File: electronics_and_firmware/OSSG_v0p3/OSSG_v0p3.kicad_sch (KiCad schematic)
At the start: 69 parts, among them IC1 DW01A, J1 USB_B_Micro, J2 External PDM Mic Input, Q1 FS8205A, Q2 Q_NPN_BEC, Q3 Q_NPN_BEC, SW1 SW_SPST, U1 ESP32-PICO-D4, U2 TP4056, U3 XC6222B331MRG, U4 CH9102F, U5 CL7809SS, U6 MP23DB01HPTR

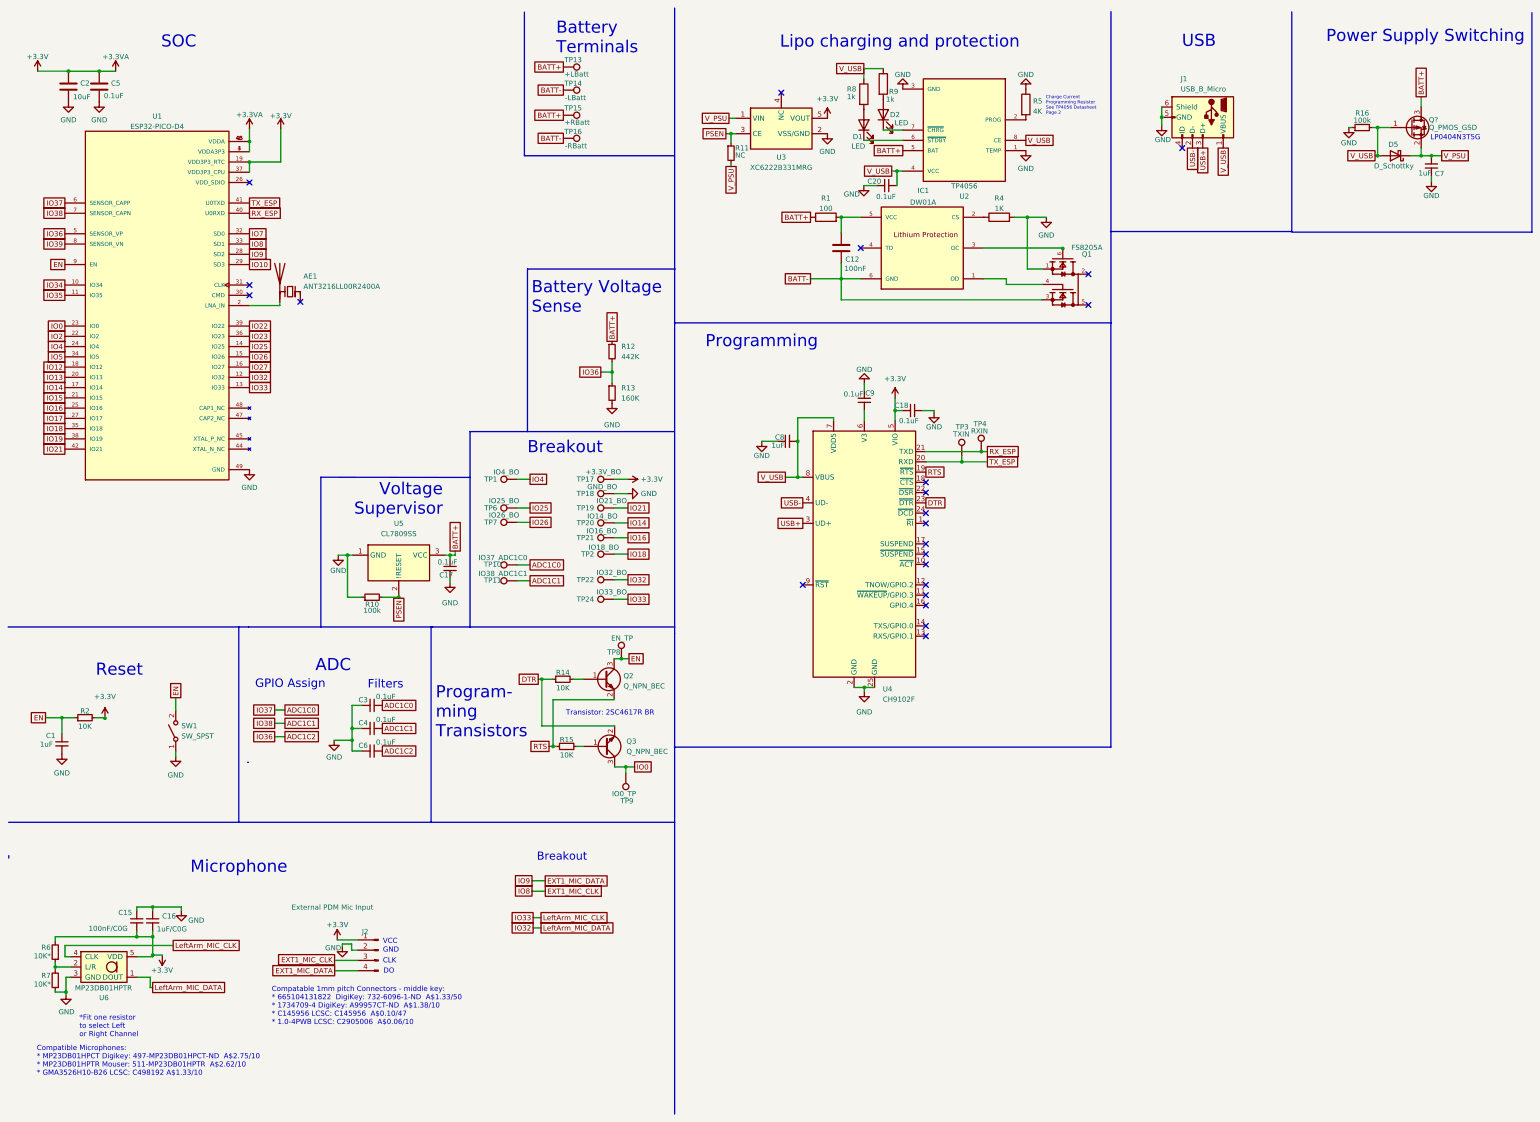
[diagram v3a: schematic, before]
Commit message: change to new LDO, change voltage supervisor, inspect board, slight silk screen changes
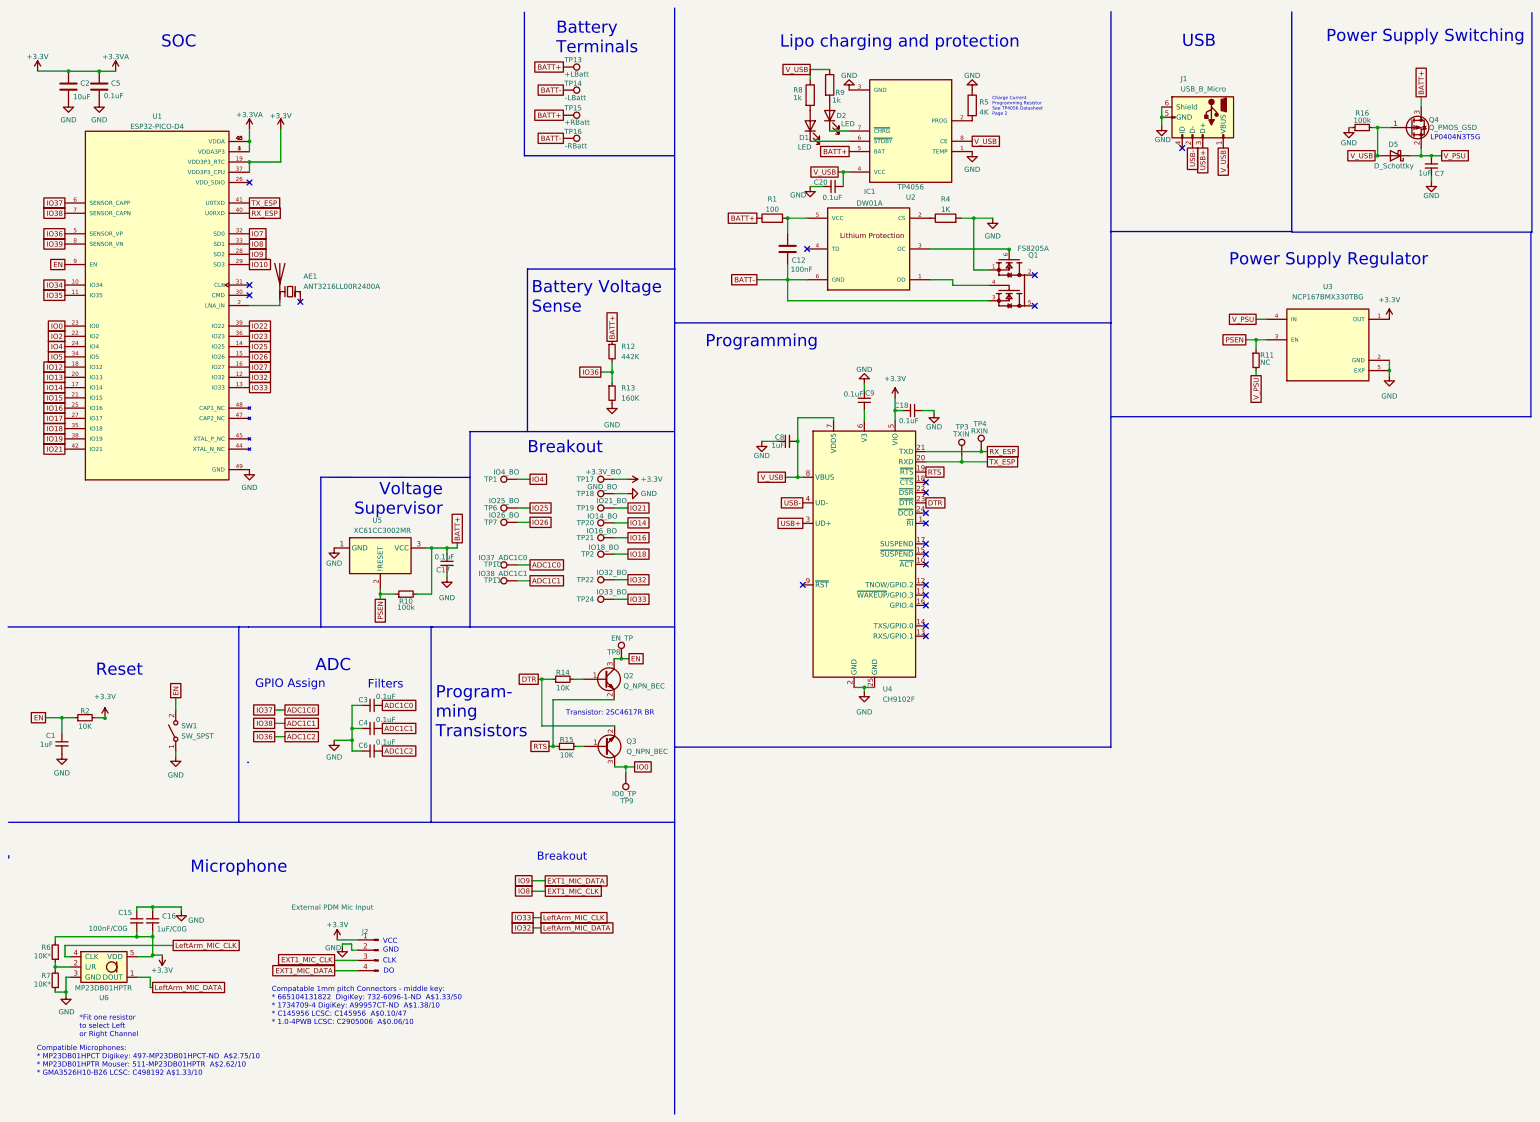
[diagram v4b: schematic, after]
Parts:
- removed U3: XC6222B331MRG, Package_TO_SOT_SMD:SOT-23-5, symbol OSSG_components_lib:XC6222B331MRG
- added U3: NCP167BMX330TBG, OSSG_footprints:REG_NCP167BMX330TBG, symbol NCP167BMX330TBG:NCP167BMX330TBG
- Q4: renamed from Q?; footprint (none) -> Package_TO_SOT_SMD:SOT-883
- U4: MPN_LCSC (none) -> C2858418; Price_LCSC (none) -> 1.35
- U5: value CL7809SS -> XC61CC3002MR; LCSCLink https://lcsc.com/product-detail/Monitors-Reset-Circuits_Chi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 -> https://lcsc.com/product-detail/Monitors-Reset-Circuits_Tor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; MPN_LCSC CL7809SS -> C80698; Price_LCSC 0.0395 -> 0.1688
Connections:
- net +3V3: now also U3.1 (OUT)
- net BATT+: now also R10.2
- net GND: now also U3.2 (GND), U3.5 (EXP); no longer R10.1
- net PSEN: now also R10.1, U3.3 (EN); no longer R10.2
- net V_PSU: now also U3.4 (IN)
- no-connect marks 22 -> 21
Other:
- note added: "Power Supply Regulator"
- moved on the sheet: C12, C17, C20, D1, D2, IC1, Q1, R1, R10, R11, R4, R5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

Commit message: change PICO gpios to use non-reserverd pins (and add reserved pins note), change FS8205A MPN to SOT-23 version, fix voltage supervisor symbol
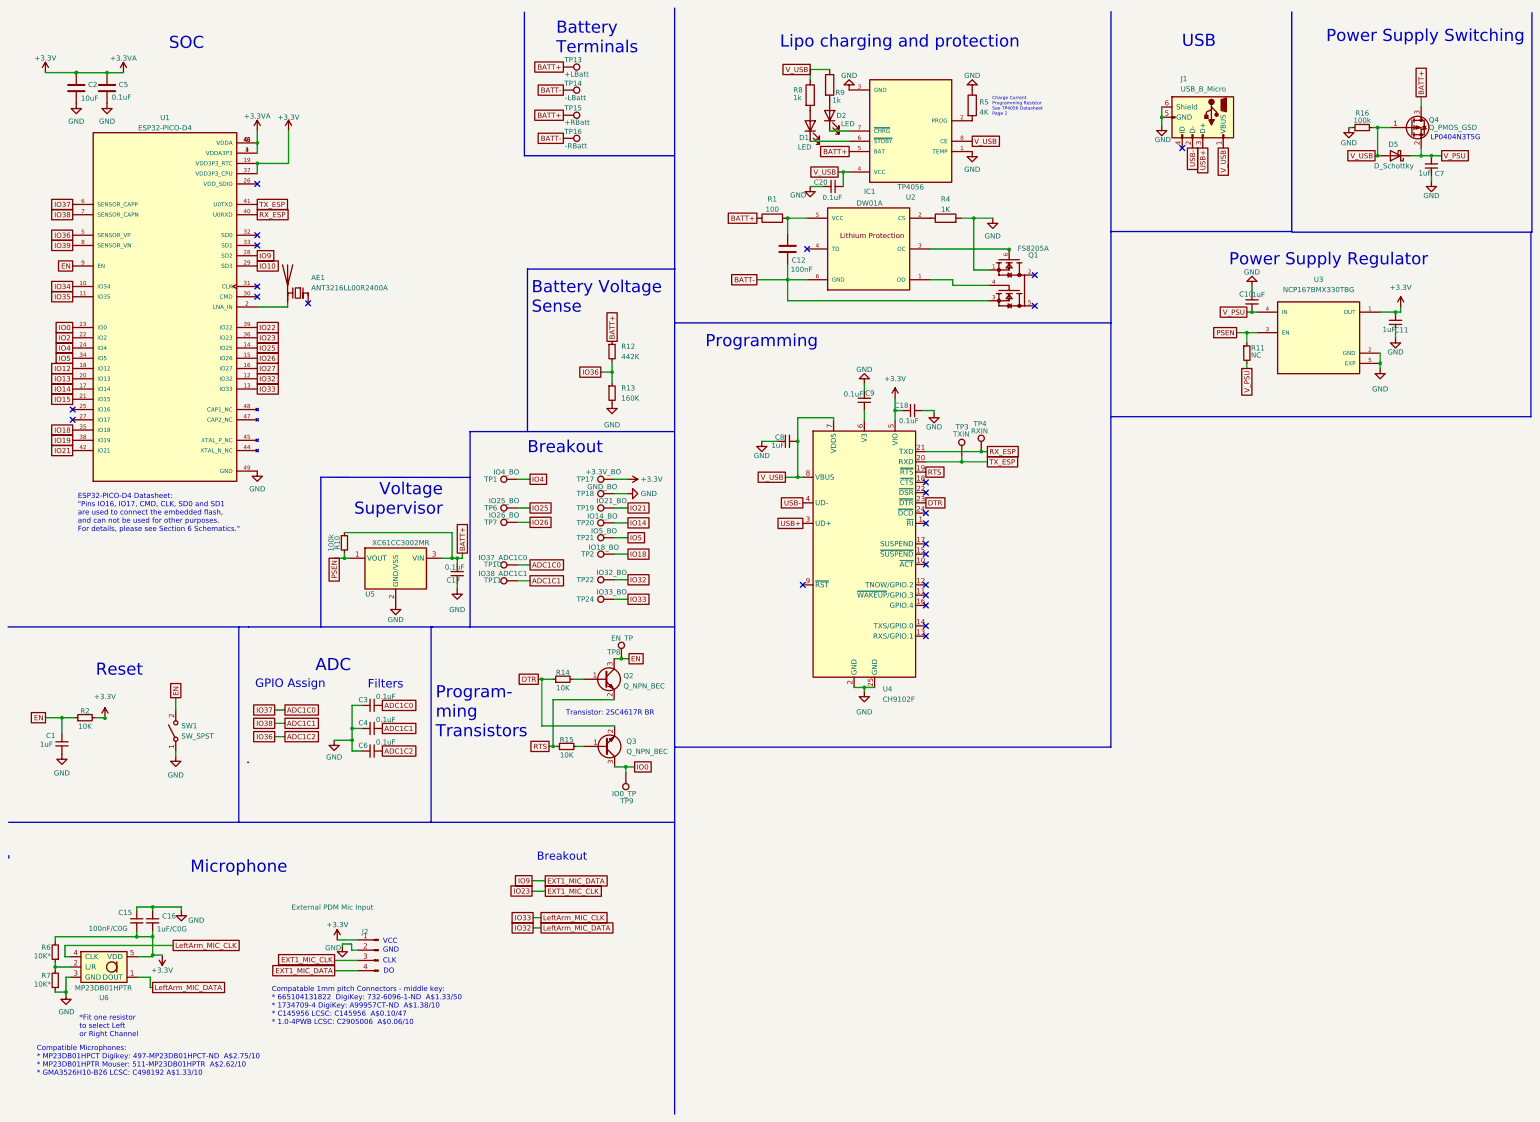
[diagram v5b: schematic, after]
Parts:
- removed U5: XC61CC3002MR, Package_TO_SOT_SMD:SOT-23, symbol OSSG_components_lib:APX803L-29SA-7
- added C10, C11: 1uF, Capacitor_SMD:C_0402_1005Metric, symbol Device:C_Small
- added U5: XC61CC3002MR, Package_TO_SOT_SMD:SOT-23, symbol OSSG_components_lib:XC61C_voltage_supervisor
- AE1: Price_LCSC 0.1212 -> 0.1226
- C15: Price_LCSC 0.0008 -> 0.0009
- D5: Price_LCSC 0.0163 -> 0.0158
- IC1: Price_LCSC 0.061 -> 0.0605
- Q1: LCSCLink https://lcsc.com/product-detail/MOSFETs_Fortune-Semicon-FS8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 -> https://www.lcsc.com/product-detail/MOSFETs_TECH-PUBLIC-FS8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; MPN_LCSC C16052 -> C2830320; Price 0.2665 -> 0.0661
- Q4: MPN_LCSC (none) -> C172433; Price_LCSC (none) -> 0.0424
- R16: MPN_LCSC C106234 -> 1
- SW1: Price_LCSSC 0.7718 -> 0.8963
- TP21: value IO16_BO -> IO5_BO
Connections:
- net IO23 is gone; now on net EXT1_MIC_CLK: U1.36 (IO23)
- net +3V3: now also C11.2
- net BATT+: now also R10.1, U5.3 (VIN); no longer R10.2
- net EXT1_MIC_CLK: no longer U1.33 (SD1)
- net GND: now also C10.1, C11.1, U5.2 (GND/VSS)
- net IO5: now also TP21.1
- net PSEN: now also R10.2, U5.1 (VOUT); no longer R10.1
- net V_PSU: now also C10.2
- net IO16: no longer names the net of U1.25 (IO16)
- net IO16: no longer TP21.1
- net IO17: no longer names the net of U1.27 (IO17)
- net IO7: no longer names the net of U1.32 (SD0)
- no-connect marks 21 -> 25
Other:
- note added: "ESP32-PICO-D4 Datasheet: "Pins IO16, IO17, CMD, CLK, SD0 and SD1 are used to connect the embedded flash, and can not be used for other purposes. For details, please see Section 6 Schematics.""
- moved on the sheet: AE1, C17, C2, C5, R10, R11, U1, U3

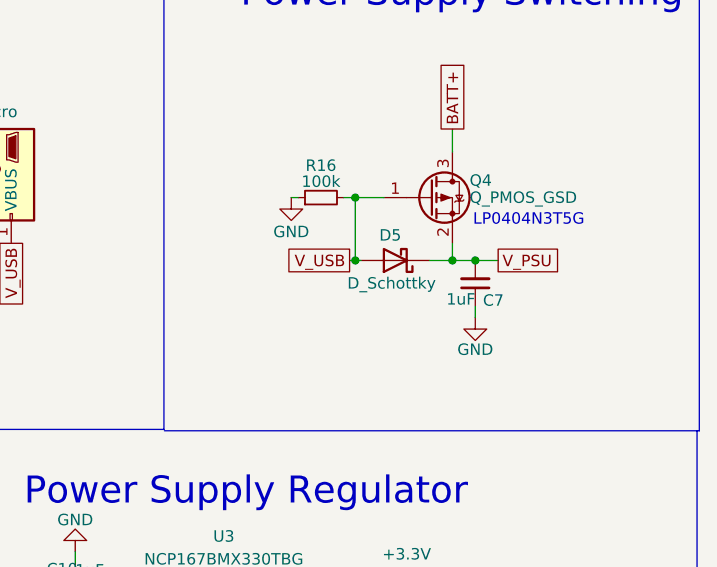
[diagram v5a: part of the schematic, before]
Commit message: update diode to 1A diode
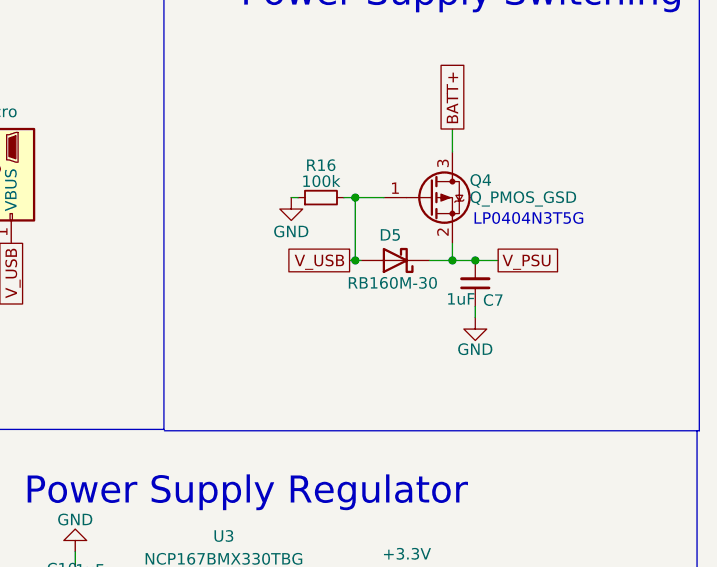
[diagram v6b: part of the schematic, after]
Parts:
- D5: value D_Schottky -> RB160M-30; footprint Diode_SMD:D_SOD-323 -> Diode_SMD:D_SOD-123; MPN_LCSC C109204 -> C2937163; Price_LCSC 0.0158 -> 0.0743
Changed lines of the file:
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@@
       (effects (font (size 1.27 1.27)) (justify right))
     )
-    (property "Value" "D_Schottky" (id 1) (at 350.266 50.165 0)
+    (property "Value" "RB160M-30" (id 1) (at 350.266 50.165 0)
       (effects (font (size 1.27 1.27)) (justify right))
     )
-    (property "Footprint" "Diode_SMD:D_SOD-323" (id 2) (at 355.6 47.625 0)
-      (effects (font (size 1.27 1.27)) hide)
-    )
-    (property "Datasheet" "https://datasheet.lcsc.com/lcsc/1809211226_Shikues-SD103AWS_C109204.pdf" (id 3) (at 355.6 47.625 0)
-      (effects (font (size 1.27 1.27)) hide)
-    )
-    (property "MPN_LCSC" "C109204" (id 4) (at 355.6 47.625 90)
-      (effects (font (size 1.27 1.27)) hide)
-    )
-    (property "Price_LCSC" "0.0158" (id 5) (at 355.6 47.625 90)
+    (property "Footprint" "Diode_SMD:D_SOD-123" (id 2) (at 355.6 47.625 0)
+      (effects (font (size 1.27 1.27)) hide)
+    )
+    (property "Datasheet" "https://datasheet.lcsc.com/lcsc/2201121800_High-Diode-RB160M-30_C2937163.pdf" (id 3) (at 355.6 47.625 0)
+      (effects (font (size 1.27 1.27)) hide)
+    )
+    (property "MPN_LCSC" "C2937163" (id 4) (at 355.6 47.625 90)
+      (effects (font (size 1.27 1.27)) hide)
+    )
+    (property "Price_LCSC" "0.0743" (id 5) (at 355.6 47.625 90)
       (effects (font (size 1.27 1.27)) hide)
     )
@@
     )
     (path "/828f1b7d-33c4-491d-afb9-0a7bfd867166"
-      (reference "D5") (unit 1) (value "D_Schottky") (footprint "Diode_SMD:D_SOD-323")
+      (reference "D5") (unit 1) (value "RB160M-30") (footprint "Diode_SMD:D_SOD-123")
     )
     (path "/fc863d10-a826-4023-a674-52ff363ca591"

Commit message: last changes before order
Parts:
- C16: footprint Capacitor_SMD:C_0402_1005Metric -> 1uF
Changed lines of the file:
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@@
       (effects (font (size 1.27 1.27)) (justify left))
     )
-    (property "Footprint" "Capacitor_SMD:C_0402_1005Metric" (id 2) (at 47.752 237.1344 0)
+    (property "Footprint" "1uF" (id 2) (at 47.752 237.1344 0)
       (effects (font (size 1.27 1.27)) hide)
     )
@@
     )
     (path "/ae917cc4-e478-450b-a388-bed3c5bb6672"
-      (reference "C16") (unit 1) (value "1uF/C0G") (footprint "Capacitor_SMD:C_0402_1005Metric")
+      (reference "C16") (unit 1) (value "1uF/C0G") (footprint "1uF")
     )
     (path "/8d6867b1-01a6-438c-add5-a9e0376be53f"
